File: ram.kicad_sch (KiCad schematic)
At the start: 20 parts, among them U19 7130, U7 74HCT245

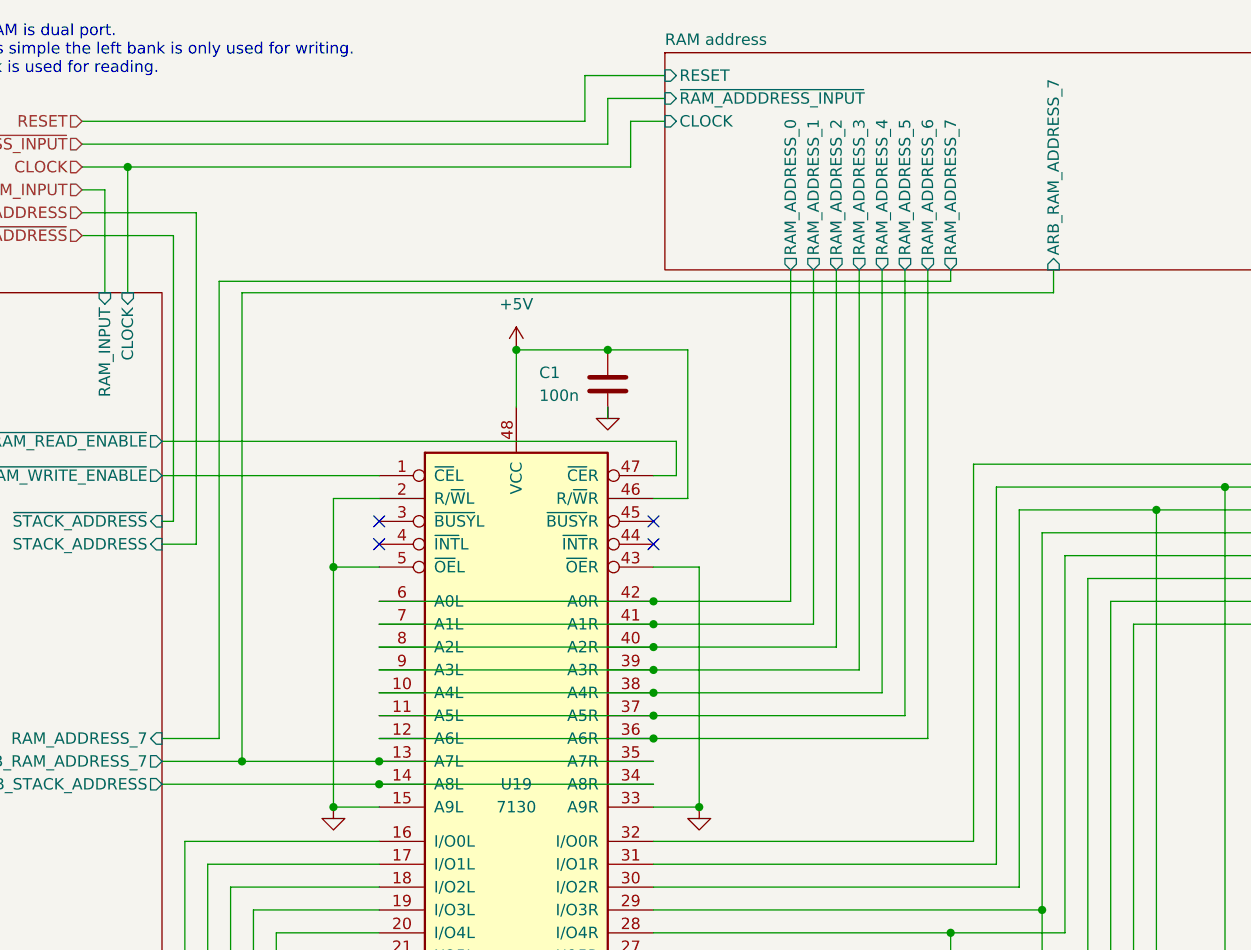
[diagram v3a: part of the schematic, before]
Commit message: changed symbols
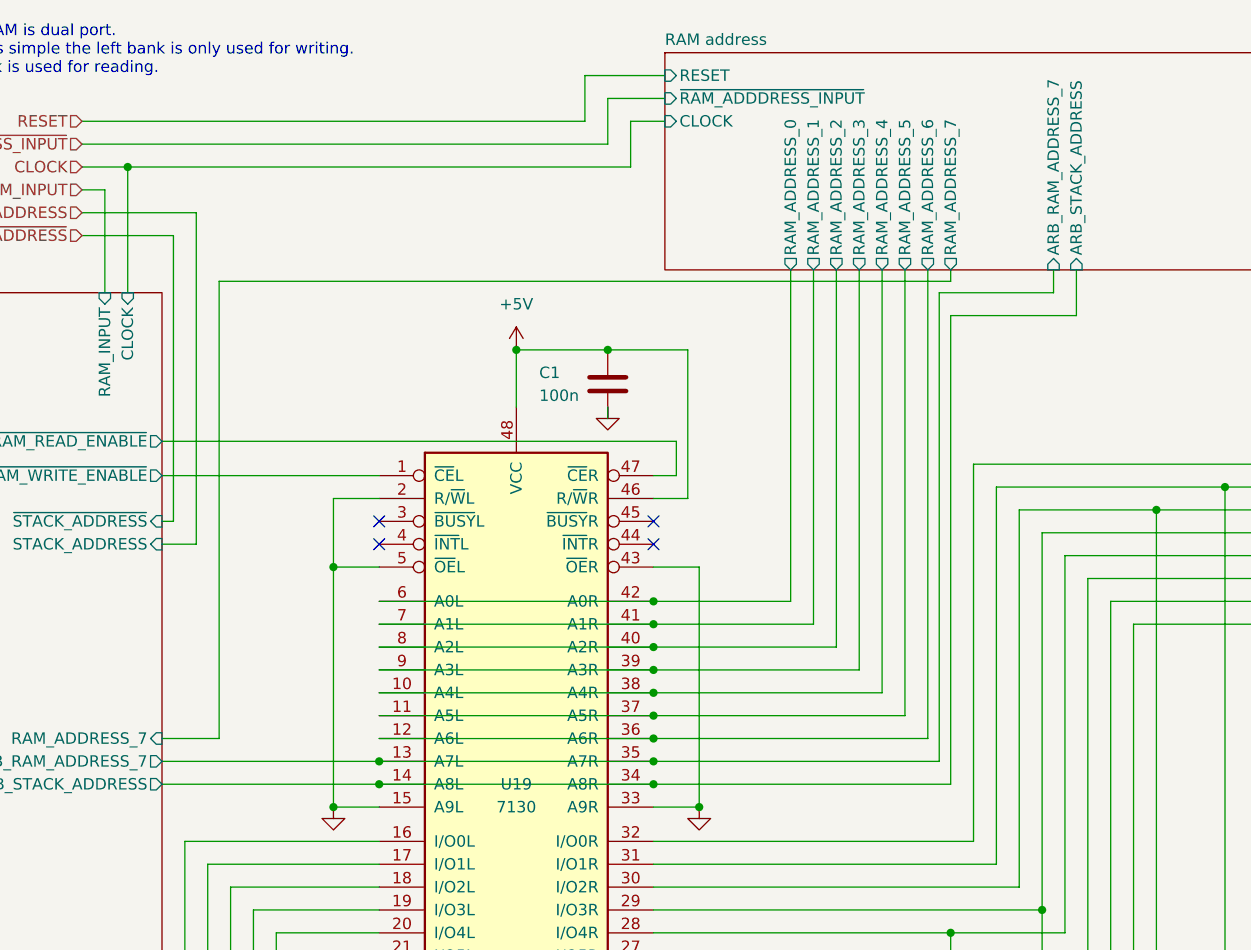
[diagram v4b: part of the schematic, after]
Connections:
- net RAM logic/ARB_STACK_ADDRESS renamed RAM address/ARB_STACK_ADDRESS
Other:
- sheet RAM address ports: added ARB_STACK_ADDRESS; removed none
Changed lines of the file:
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@@
   (junction (at 63.5 73.66) (diameter 0) (color 0 0 0 0)
   )
-  (junction (at 53.34 95.25) (diameter 0) (color 0 0 0 0)
-  )
   (junction (at 99.06 85.09) (diameter 0) (color 0 0 0 0)
   )
@@
   (junction (at 63.5 100.33) (diameter 0) (color 0 0 0 0)
   )
+  (junction (at 99.06 95.25) (diameter 0) (color 0 0 0 0)
+  )
   (junction (at 247.65 80.01) (diameter 0) (color 0 0 255 1)
   )
   (junction (at 251.46 80.01) (diameter 0) (color 0 0 255 1)
   )
+  (junction (at 99.06 97.79) (diameter 0) (color 0 0 0 0)
+  )
   (junction (at 154.94 67.31) (diameter 0) (color 0 0 0 0)
   )
@@
   (junction (at 245.11 77.47) (diameter 0) (color 0 0 255 1)
   )
-  (junction (at 68.58 97.79) (diameter 0) (color 255 0 0 1)
+  (junction (at 68.58 97.79) (diameter 0) (color 0 0 0 0)
   )
   (junction (at 269.24 62.23) (diameter 0) (color 0 0 255 1)
@@
     (stroke (width 0) (type default))
   )
+  (wire (pts (xy 146.05 45.72) (xy 132.08 45.72))
+    (stroke (width 0) (type default))
+  )
   (wire (pts (xy 129.54 92.71) (xy 99.06 92.71))
     (stroke (width 0) (type default))
@@
     (stroke (width 0) (type default) (color 0 0 255 1))
   )
-  (wire (pts (xy 44.45 95.25) (xy 53.34 95.25))
+  (wire (pts (xy 130.81 95.25) (xy 99.06 95.25))
     (stroke (width 0) (type default))
   )
@@
     (stroke (width 0) (type default))
   )
+  (wire (pts (xy 146.05 40.64) (xy 146.05 45.72))
+    (stroke (width 0) (type default))
+  )
   (wire (pts (xy 135.89 163.83) (xy 135.89 156.21))
     (stroke (width 0) (type default) (color 0 0 255 1))
@@
     (stroke (width 0) (type default))
   )
+  (wire (pts (xy 132.08 45.72) (xy 132.08 97.79))
+    (stroke (width 0) (type default))
+  )
   (wire (pts (xy 142.24 146.05) (xy 152.4 146.05))
     (stroke (width 0) (type default))
@@
     (stroke (width 0) (type default) (color 0 0 255 1))
   )
+  (wire (pts (xy 44.45 97.79) (xy 68.58 97.79))
+    (stroke (width 0) (type default))
+  )
   (wire (pts (xy 125.73 168.91) (xy 140.97 168.91))
     (stroke (width 0) (type default) (color 0 0 255 1))
@@
   )
   (wire (pts (xy 68.58 97.79) (xy 99.06 97.79))
-    (stroke (width 0) (type default) (color 255 0 0 1))
+    (stroke (width 0) (type default))
   )
   (wire (pts (xy 198.12 29.21) (xy 259.08 29.21))
@@
     (stroke (width 0) (type default))
   )
-  (wire (pts (xy 53.34 95.25) (xy 68.58 95.25))
+  (wire (pts (xy 44.45 95.25) (xy 68.58 95.25))
     (stroke (width 0) (type default))
   )
@@
     (stroke (width 0) (type default))
   )
+  (wire (pts (xy 130.81 43.18) (xy 130.81 95.25))
+    (stroke (width 0) (type default))
+  )
   (wire (pts (xy 40.64 29.21) (xy 40.64 43.18))
     (stroke (width 0) (type default) (color 255 0 0 1))
@@
     (stroke (width 0) (type default) (color 255 0 0 1))
   )
-  (wire (pts (xy 143.51 43.18) (xy 53.34 43.18))
-    (stroke (width 0) (type default))
-  )
   (wire (pts (xy 256.54 31.75) (xy 256.54 74.93))
     (stroke (width 0) (type default) (color 0 0 255 1))
@@
     (stroke (width 0) (type default) (color 255 0 0 1))
   )
-  (wire (pts (xy 53.34 43.18) (xy 53.34 95.25))
-    (stroke (width 0) (type default))
-  )
   (wire (pts (xy 116.84 80.01) (xy 116.84 40.64))
     (stroke (width 0) (type default))
@@
     (stroke (width 0) (type default))
   )
-  (wire (pts (xy 44.45 97.79) (xy 68.58 97.79))
-    (stroke (width 0) (type default) (color 255 0 0 1))
-  )
   (wire (pts (xy 186.69 90.17) (xy 193.04 90.17))
     (stroke (width 0) (type default))
@@
     (stroke (width 0) (type default))
   )
+  (wire (pts (xy 132.08 97.79) (xy 99.06 97.79))
+    (stroke (width 0) (type default))
+  )
   (wire (pts (xy 245.11 77.47) (xy 245.11 166.37))
     (stroke (width 0) (type default) (color 0 0 255 1))
@@
   )
   (wire (pts (xy 68.58 90.17) (xy 99.06 90.17))
+    (stroke (width 0) (type default))
+  )
+  (wire (pts (xy 143.51 43.18) (xy 130.81 43.18))
     (stroke (width 0) (type default))
   )
@@
       (effects (font (size 1.27 1.27)) (justify left))
     )
+    (pin "ARB_STACK_ADDRESS" input (at 146.05 40.64 270)
+      (effects (font (size 1.27 1.27)) (justify left))
+    )

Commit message: some cleanup
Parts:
- U7: symbol 74xx:74HC245 -> 01_my_library:74HCT245
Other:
- note added: "This is wired in reverse on the breadboard. DIR is tied to ground. Not changing the schematic because it does not matter."
- note removed: "This is wired in reverse on the breadboard. A->B is tied to ground. Not changing the schematic because it does not matter."
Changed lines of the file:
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@@
     (stroke (width 0) (type default) (color 0 0 255 1))
   )
-  (text "This is wired in reverse\non the breadboard.\nA->B is tied to ground.\nNot changing the schematic\nbecause it does not matter."
+  (text "This is wired in reverse\non the breadboard.\nDIR is tied to ground.\nNot changing the schematic\nbecause it does not matter."
     (at 196.85 111.76 0)
     (effects (font (size 1.27 1.27)) (justify left bottom))
@@
     )
   )
-  (symbol (lib_id "74xx:74HC245") (at 208.28 74.93 0) (unit 1)
+  (symbol (lib_id "01_my_library:74HCT245") (at 208.28 74.93 0) (unit 1)
     (in_bom yes) (on_board yes) (dnp no)
     (property "Reference" "U7" (at 220.98 82.55 0)
@@
       (effects (font (size 1.27 1.27)) hide)
     )
-    (property "Datasheet" "http://www.ti.com/lit/gpn/sn74HC245" (at 208.28 74.93 0)
-      (effects (font (size 1.27 1.27)) hide)
-    )
+    (property "Datasheet" "https://www.ti.com/lit/ds/symlink/sn74hct245.pdf?ts=1702763405638&ref_url=https%253A%252F%252Fwww.google.com%252F" (at 208.28 97.79 0)
+      (effects (font (size 1.27 1.27)) hide)
+    )
